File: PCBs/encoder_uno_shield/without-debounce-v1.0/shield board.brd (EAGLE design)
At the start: 70.6 x 53.8 mm, 13 parts, among them U1 ARDUINOR3-BPLACE

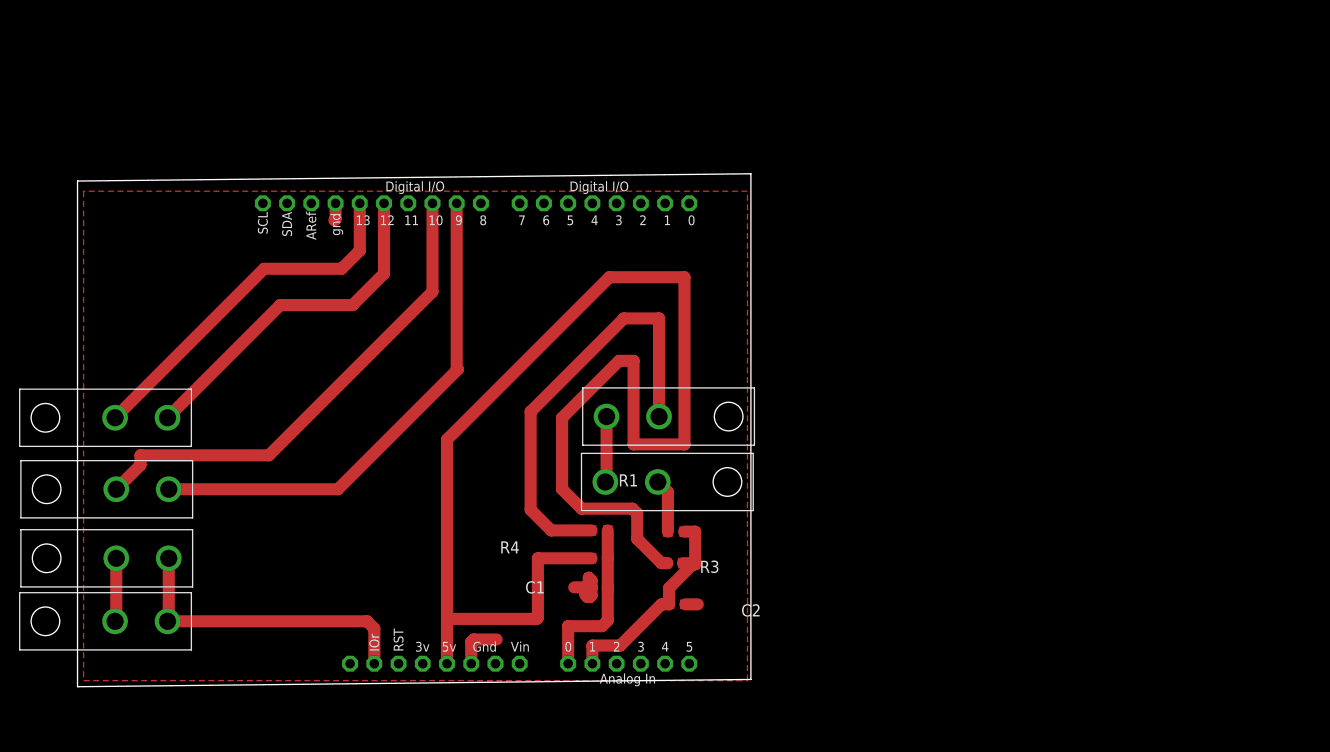
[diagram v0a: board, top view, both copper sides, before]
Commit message: realized i only need one switch port, about to redesign
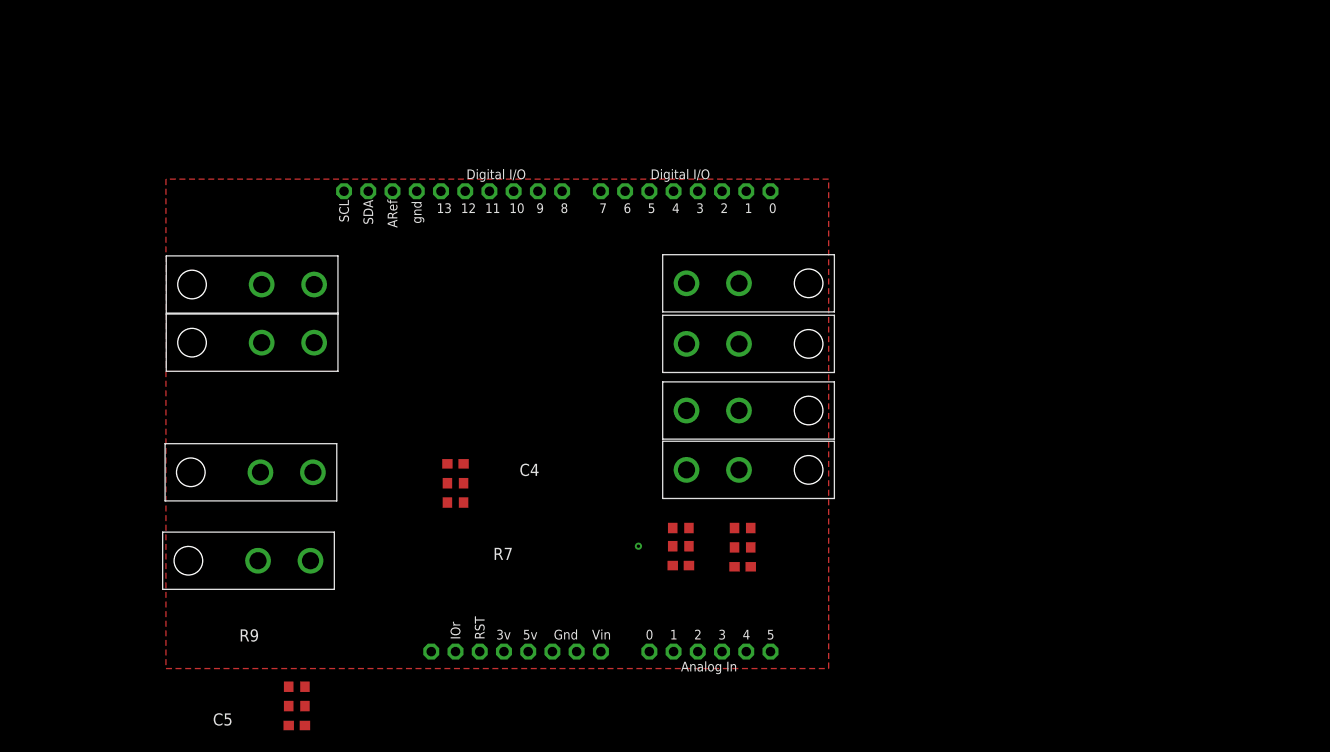
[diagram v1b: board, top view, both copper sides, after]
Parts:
- added C4, C5: 0.1uF, adafruit:C0603
- added R10, R8: 10k, resistor:R0603
- added R7, R9: 1k, resistor:R0603
- added U$7, U$8: MOLEX_0039301022, pat:MINI-FIT_JR_CONN
- moved U$3 74.4 mm to (68.7, 42.4), turned to 90 degrees
- moved U$6 67.0 mm to (68.7, 36.1), turned to 90 degrees
- moved U$4 27.3 mm to (18.7, 36.2)
- moved U$5 20.8 mm to (18.7, 42.3)
- moved C1 8.81 mm to (62.6, 12.8)
- moved R4 8.60 mm to (62.6, 14.9)
- moved U1 8.60 mm to (8.51, 1.27)
- moved U$1 8.60 mm to (68.7, 22.9)
- moved R3 8.51 mm to (62.6, 16.8)
- moved U$2 8.41 mm to (68.7, 29.1)
- moved C2 7.91 mm to (69.1, 12.7)
- moved R2 7.30 mm to (69.1, 14.7)
- moved R1 7.00 mm to (69.1, 16.8)
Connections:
- net SW_X renamed YSW1
- net SW_Y renamed YSW2
- new net 5V: R10.2, R8.2
- new net N$3: R7.1, U$7.P$1
- new net N$5: R9.1, U$8.P$1
- new net XSW1: C4.1, R7.2, R8.1
- new net XSW2: C5.1, R10.1, R9.2
- net GND: now also C4.2, C5.2, U$7.P$2, U$8.P$2
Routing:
- net VCC: track 178.8 -> 0.00 mm, vias 0 -> 1
- net E2CHA: track 53.0 -> 0.00 mm
- net E2CHB: track 51.6 -> 0.00 mm
- net N$4: track 45.4 -> 0.00 mm
- net E1CHB: track 37.9 -> 0.00 mm
- net E1CHA: track 36.3 -> 0.00 mm
- net YSW2: track 23.1 -> 0.00 mm
- net GND: track 22.7 -> 0.00 mm
- net YSW1: track 17.8 -> 0.00 mm
- net N$1: track 5.64 -> 0.00 mm
- net GND2: track 5.06 -> 0.00 mm
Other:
- board outline removed

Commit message: routed new board design
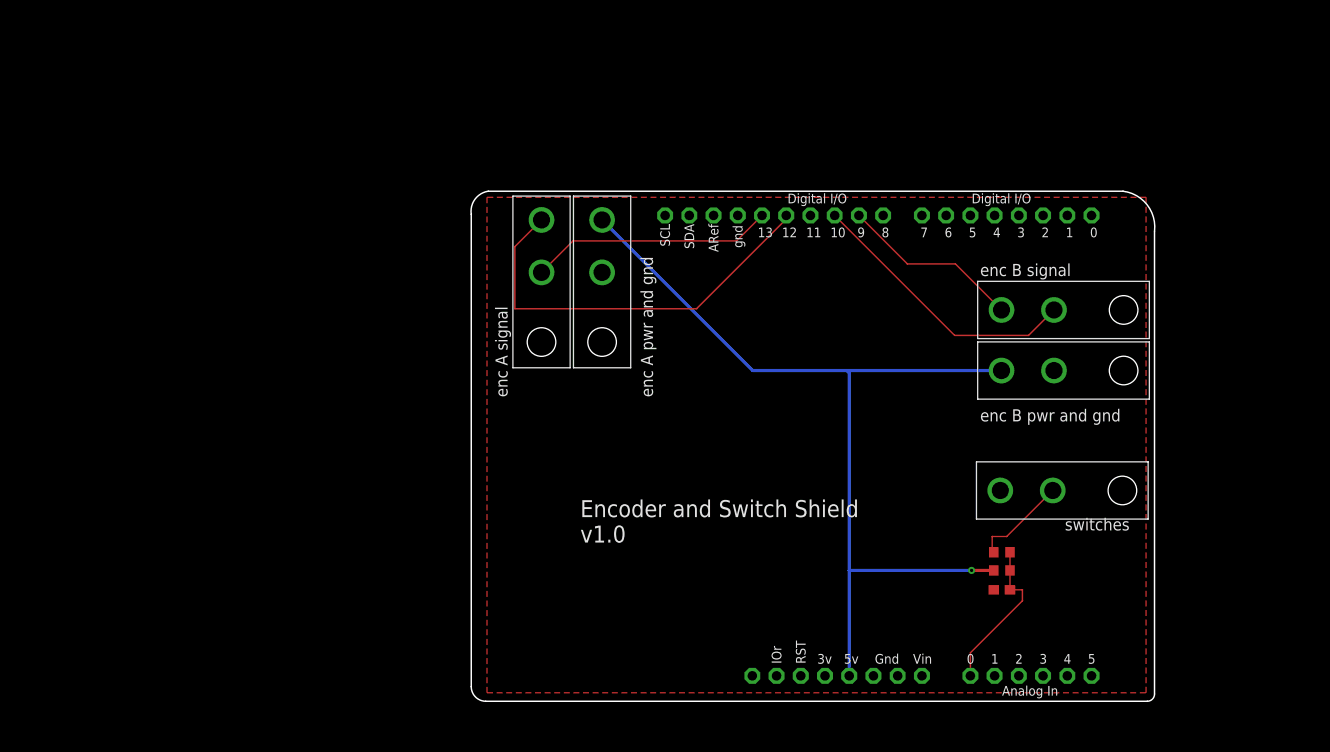
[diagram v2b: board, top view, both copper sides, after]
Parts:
- removed C2, C4, C5: 0.1uF, adafruit:C0603
- removed R1, R7, R9: 1k, resistor:R0603
- removed R10, R2, R8: 10k, resistor:R0603
- removed U$1, U$7, U$8: MOLEX_0039301022, pat:MINI-FIT_JR_CONN
- moved U$4 36.4 mm to (54.4, 43.6), turned to 0 degrees
- moved U$3 34.3 mm to (101.7, 33.3)
- moved U$2 33.9 mm to (101.6, 20.7)
- moved C1 33.8 mm to (96.3, 10.3)
- moved R3 33.8 mm to (96.3, 14.2)
- moved R4 33.8 mm to (96.3, 12.3)
- moved U1 33.8 mm to (42.2, -1.27)
- moved U$6 33.2 mm to (101.7, 39.6)
- moved U$5 29.4 mm to (48.0, 43.6), turned to 0 degrees
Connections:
- net YSW1 renamed SWITCH
- removed net 5V: R10.2, R8.2
- removed net N$1: R1.1, U$1.P$1
- removed net N$3: R7.1, U$7.P$1
- removed net N$5: R9.1, U$8.P$1
- removed net XSW1: C4.1, R7.2, R8.1
- removed net XSW2: C5.1, R10.1, R9.2
- removed net YSW2: C2.1, R1.2, R2.1, U1.A1
- net GND: no longer C2.2, C4.2, C5.2, U$1.P$2, U$7.P$2, U$8.P$2
- net VCC: no longer R2.2
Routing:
- net VCC: track 0.00 -> 95.7 mm
- net E1CHA: track 0.00 -> 43.2 mm
- net E2CHB: track 0.00 -> 29.3 mm
- net E1CHB: track 0.00 -> 25.6 mm
- net E2CHA: track 0.00 -> 19.1 mm
- net SWITCH: track 0.00 -> 16.5 mm
- net N$4: track 0.00 -> 10.1 mm
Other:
- board outline added: 71.7 x 53.5 mm
- board text added: "Encoder and Switch Shield v1.0"
- board text added: "enc A pwr and gnd"
- board text added: "enc A signal"
- board text added: "enc B pwr and gnd"
- board text added: "enc B signal"
- board text added: "switches"

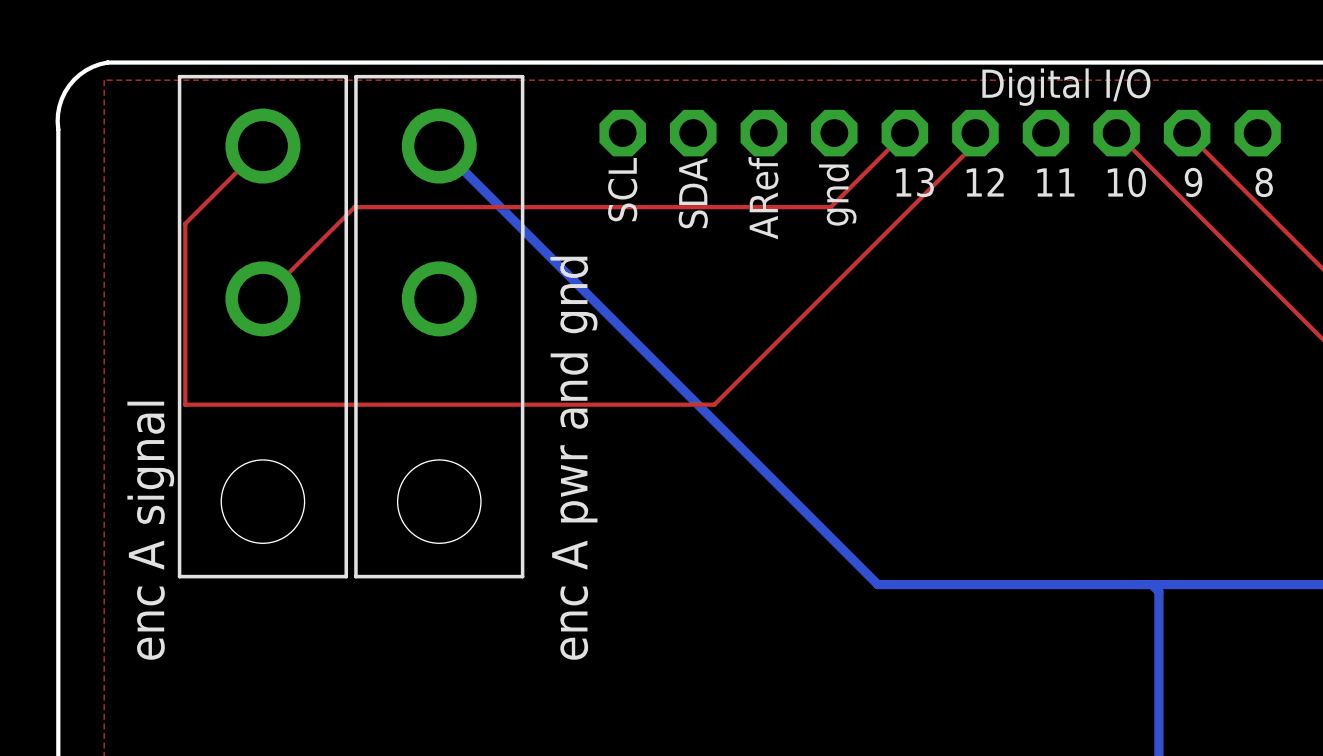
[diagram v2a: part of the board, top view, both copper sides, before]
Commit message: fixed orientation of molex connectors in encoder shield
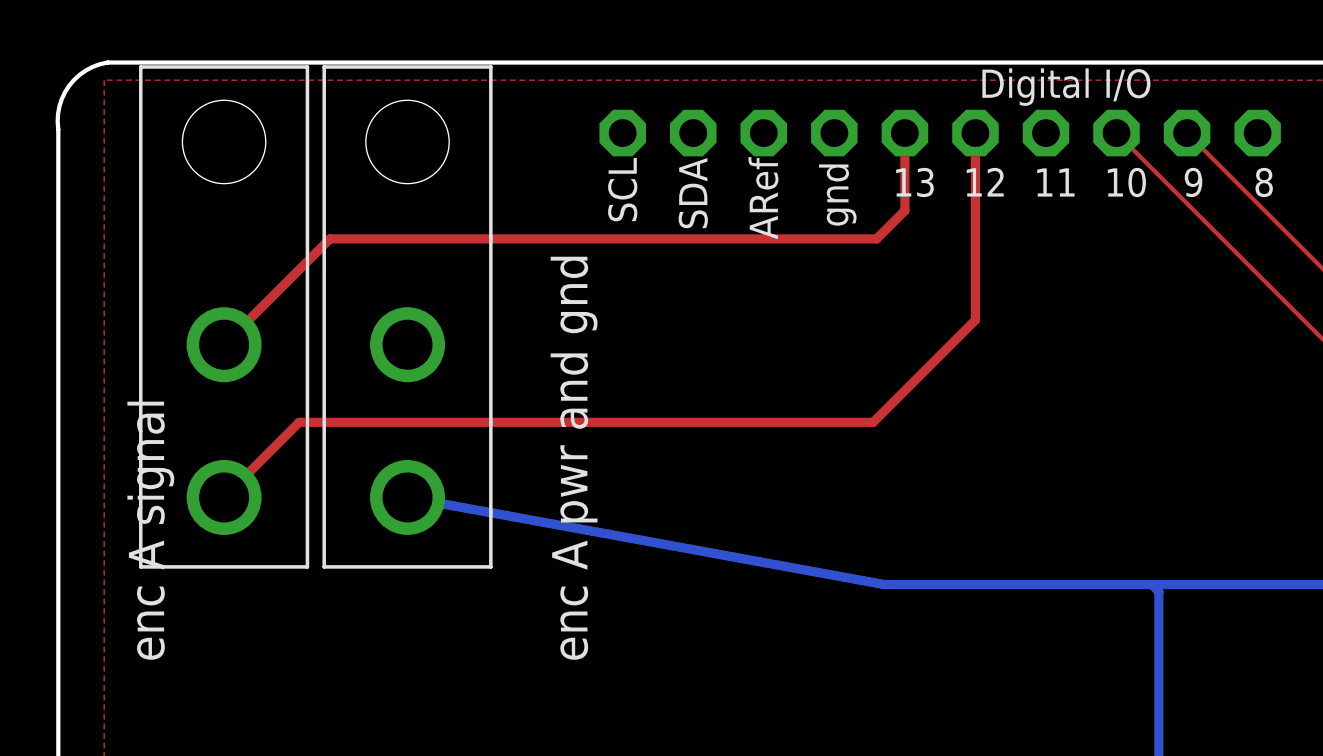
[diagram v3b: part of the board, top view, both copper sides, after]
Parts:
- moved U$5 2.16 mm to (46.6, 41.9), turned to 180 degrees
- moved U$4 2.01 mm to (53.2, 41.9), turned to 180 degrees
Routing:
- net E1CHA: track 43.2 -> 36.8 mm
- net VCC: track 95.7 -> 90.6 mm
- net E1CHB: track 25.6 -> 29.3 mm
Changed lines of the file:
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@@
 <element name="U$2" library="pat" package="MINI-FIT_JR_CONN" value="MOLEX_0039301022" x="101.6" y="20.701" smashed="yes" rot="R90"/>
 <element name="U$3" library="pat" package="MINI-FIT_JR_CONN" value="MOLEX_0039301022" x="101.727" y="33.274" smashed="yes" rot="R90"/>
-<element name="U$4" library="pat" package="MINI-FIT_JR_CONN" value="MOLEX_0039301022" x="54.356" y="43.561" smashed="yes"/>
-<element name="U$5" library="pat" package="MINI-FIT_JR_CONN" value="MOLEX_0039301022" x="48.006" y="43.561" smashed="yes"/>
+<element name="U$4" library="pat" package="MINI-FIT_JR_CONN" value="MOLEX_0039301022" x="53.213" y="41.91" smashed="yes" rot="R180"/>
+<element name="U$5" library="pat" package="MINI-FIT_JR_CONN" value="MOLEX_0039301022" x="46.609" y="41.91" smashed="yes" rot="R180"/>
 <element name="U$6" library="pat" package="MINI-FIT_JR_CONN" value="MOLEX_0039301022" x="101.727" y="39.624" smashed="yes" rot="R90"/>
 </elements>
@@
 <contactref element="U$3" pad="P$2"/>
 <contactref element="U$4" pad="P$2"/>
-<wire x1="70.143" y1="33.274" x2="54.356" y2="49.061" width="0.3302" layer="16"/>
+<wire x1="70.391359375" y1="33.274" x2="53.213" y2="36.41" width="0.3302" layer="16"/>
 <wire x1="96.227" y1="33.274" x2="80.01" y2="33.274" width="0.3302" layer="16"/>
-<wire x1="80.01" y1="33.274" x2="70.143" y2="33.274" width="0.3302" layer="16"/>
+<wire x1="80.01" y1="33.274" x2="70.391359375" y2="33.274" width="0.3302" layer="16"/>
 <wire x1="80.264" y1="1.27" x2="80.264" y2="12.319" width="0.3302" layer="16"/>
 <wire x1="80.264" y1="12.319" x2="80.264" y2="33.02" width="0.3302" layer="16"/>
@@
 <contactref element="U1" pad="D12"/>
 <contactref element="U$5" pad="P$2"/>
-<wire x1="48.006" y1="49.061" x2="45.212" y2="46.267" width="0.1524" layer="1"/>
-<wire x1="45.212" y1="46.267" x2="45.212" y2="39.751" width="0.1524" layer="1"/>
-<wire x1="45.212" y1="39.751" x2="64.262" y2="39.751" width="0.1524" layer="1"/>
-<wire x1="64.262" y1="39.751" x2="73.66" y2="49.149" width="0.1524" layer="1"/>
 <wire x1="73.66" y1="49.149" x2="73.66" y2="49.53" width="0.1524" layer="1"/>
+<wire x1="46.609" y1="36.41" x2="49.315" y2="39.116" width="0.3302" layer="1"/>
+<wire x1="73.66" y1="42.799" x2="73.66" y2="49.53" width="0.3302" layer="1"/>
+<wire x1="49.315" y1="39.116" x2="69.977" y2="39.116" width="0.3302" layer="1"/>
+<wire x1="69.977" y1="39.116" x2="73.66" y2="42.799" width="0.3302" layer="1"/>
 </signal>
 <signal name="E1CHB">
 <contactref element="U1" pad="D13"/>
 <contactref element="U$5" pad="P$1"/>
-<wire x1="48.006" y1="43.561" x2="51.308" y2="46.863" width="0.1524" layer="1"/>
-<wire x1="68.453" y1="46.863" x2="71.12" y2="49.53" width="0.1524" layer="1"/>
-<wire x1="51.308" y1="46.863" x2="68.453" y2="46.863" width="0.1524" layer="1"/>
+<wire x1="46.609" y1="41.91" x2="50.419" y2="45.72" width="0.3302" layer="1"/>
+<wire x1="50.419" y1="45.72" x2="70.104" y2="45.72" width="0.3302" layer="1"/>
+<wire x1="70.104" y1="45.72" x2="71.12" y2="46.736" width="0.3302" layer="1"/>
+<wire x1="71.12" y1="46.736" x2="71.12" y2="49.53" width="0.3302" layer="1"/>
 </signal>
 <signal name="E2CHB">
